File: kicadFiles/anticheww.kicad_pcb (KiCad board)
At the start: 2 copper layers, 303.2 x 94.2 mm, 154 parts, among them J1 TYPE-C-31-M12_13, SW1 ESC, SW10 9, SW11 0, SW12 MINUS, SW13 PLUS, SW14 LBKSP, SW15 RBKSP, SW16 PGUP, SW17 2U_BKSP, SW18 TAB, SW19 Q, SW2 1, SW20 W, SW21 E, SW22 R, SW23 T, SW24 Y, SW25 U, SW26 I, SW27 O, SW28 P, SW29 LBRKT, SW3 2, SW30 RBRKT, SW31 BKSLSH, SW32 PGDN, SW33 CAPS, SW34 A, SW35 S, SW36 D, SW37 F, SW38 G, SW39 H, SW4 3, SW40 J, SW41 K, SW42 L, SW43 COLON, SW44 QUOTE, SW45 ENTER, SW46 HOME, SW47 LSHFT, SW48 STEPPED_CAPS, SW49 Z, SW5 4, SW50 X, SW51 C, SW52 V, SW53 B, SW54 N, SW55 M, SW56 COMMA, SW57 DOT, SW58 175_RSHFT, SW59 UP, SW6 5, SW60 END, SW61 SLSH, SW62 LCTRL, SW63 LGUI, SW64 LALT, SW65 SPC, SW66 RALT, SW67 RGUI, SW68 RCTRL, SW69 LEFT, SW7 6, SW70 DOWN, SW71 RIGHT, SW72 LCTRL, SW73 LGUI, SW74 LALT, SW75 SPC, SW8 7, SW9 8

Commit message: Route USB data lines
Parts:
- added U1: TPD4E05U06DQAR, acheron_Components:USON-10_2.5x1.0mm_P0.5mm, F.Cu at (337.2, 92.4)
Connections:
- J1 pad A6: Net-(J1-PadA6) -> D+
- J1 pad A7: Net-(J1-PadA7) -> D-
- J1 pad B6: Net-(J1-PadB6) -> D+
- J1 pad B7: Net-(J1-PadB7) -> D-
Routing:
- net D-: track 0.00 -> 32.9 mm, vias 0 -> 2
- net D+: track 0.00 -> 30.6 mm, vias 0 -> 2
- net Net-(J1-PadS): track 0.00 -> 17.0 mm
- net GND: track 0.00 -> 5.02 mm, vias 0 -> 3
- added copper zone on B.Cu, net GND
- added copper zone on F.Cu, net GND
- removed copper zone on B.Cu, net (none)
- removed copper zone on F.Cu, net (none)

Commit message: Add RGB
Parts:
- added C1: 100n, Capacitor_SMD:C_0805_2012Metric, F.Cu at (485.9, 334.5)
- added C10: 100n, Capacitor_SMD:C_0805_2012Metric, F.Cu at (287.8, 257.6)
- added C11: 100n, Capacitor_SMD:C_0805_2012Metric, F.Cu at (283.4, 257.6)
- added C12: 100n, Capacitor_SMD:C_0805_2012Metric, F.Cu at (292.2, 257.6)
- added C13: 100n, Capacitor_SMD:C_0805_2012Metric, F.Cu at (283.4, 269.4)
- added C14: 100n, Capacitor_SMD:C_0805_2012Metric, F.Cu at (274.4, 272.3)
- added C2: 100n, Capacitor_SMD:C_0805_2012Metric, F.Cu at (481.5, 340.4)
- added C3: 100n, Capacitor_SMD:C_0805_2012Metric, F.Cu at (477.5, 347.8)
- added C4: 100n, Capacitor_SMD:C_0805_2012Metric, F.Cu at (456.3, 354.4)
- added C5: 100n, Capacitor_SMD:C_0805_2012Metric, F.Cu at (485.9, 340.4)
- added C6: 100n, Capacitor_SMD:C_0805_2012Metric, F.Cu at (485.9, 337.5)
- added C7: 100n, Capacitor_SMD:C_0805_2012Metric, F.Cu at (481.5, 337.5)
- added C8: 100n, Capacitor_SMD:C_0805_2012Metric, F.Cu at (287.8, 260.5)
- added C9: 100n, Capacitor_SMD:C_0805_2012Metric, F.Cu at (283.4, 263.5)
- added D47: 1N4148W, acheron_Components:D_SOD-123, F.Cu at (373.7, 172.5)
- added D71: WS2812C, acheron_Components:LED_WS2812B_5.0x5.0mm_P3.2mm, F.Cu at (317.6, 100.9)
- added D72: WS2812C, acheron_Components:LED_WS2812B_5.0x5.0mm_P3.2mm, F.Cu at (279.5, 100.9)
- added D73: WS2812C, acheron_Components:LED_WS2812B_5.0x5.0mm_P3.2mm, F.Cu at (241.4, 100.9)
- added D74: WS2812C, acheron_Components:LED_WS2812B_5.0x5.0mm_P3.2mm, F.Cu at (203.3, 100.9)
- added D75: WS2812C, acheron_Components:LED_WS2812B_5.0x5.0mm_P3.2mm, F.Cu at (165.2, 100.9)
- added D76: WS2812C, acheron_Components:LED_WS2812B_5.0x5.0mm_P3.2mm, F.Cu at (117.6, 100.9)
- added D77: WS2812C, acheron_Components:LED_WS2812B_5.0x5.0mm_P3.2mm, F.Cu at (86.6, 100.9)
- added D78: WS2812C, acheron_Components:LED_WS2812B_5.0x5.0mm_P3.2mm, F.Cu at (85.4, 158.1)
- added D79: WS2812C, acheron_Components:LED_WS2812B_5.0x5.0mm_P3.2mm, F.Cu at (117.6, 158.1)
- added D80: WS2812C, acheron_Components:LED_WS2812B_5.0x5.0mm_P3.2mm, F.Cu at (165.2, 158.1)
- added D81: WS2812C, acheron_Components:LED_WS2812B_5.0x5.0mm_P3.2mm, F.Cu at (203.3, 158.1)
- added D82: WS2812C, acheron_Components:LED_WS2812B_5.0x5.0mm_P3.2mm, F.Cu at (241.4, 158.1)
- added D83: WS2812C, acheron_Components:LED_WS2812B_5.0x5.0mm_P3.2mm, F.Cu at (281.9, 158.1)
- added D84: WS2812C, acheron_Components:LED_WS2812B_5.0x5.0mm_P3.2mm, F.Cu at (315.2, 158.1)
- added FB1: CBG201209U121T, Inductor_SMD:L_0805_2012Metric, F.Cu at (331.8, 96.2)
- added FB2: CBG201209U121T, Inductor_SMD:L_0805_2012Metric, F.Cu at (341.6, 97.2)
- added GR1: Warning Sign (ISO Enter + LED), acheron_Graphics:warning_sign_3.6x3.2mm, F.Cu at (89.1, 115.0)
- added GR2: Warning Sign (Backspace), acheron_Graphics:warning_sign_3.6x3.2mm, F.Cu at (72.7, 84.5)
- added GR3: Warning Sign (ANSI Enter + ISO Backslash), acheron_Graphics:warning_sign_3.6x3.2mm, F.Cu at (98.7, 120.6)
- added GR4: Warning Sign (7U Space), acheron_Graphics:warning_sign_3.6x3.2mm, F.Cu at (151.4, 173.9)
- added GR5: Warning Sign (Left shift), acheron_Graphics:warning_sign_3.6x3.2mm, F.Cu at (318.0, 139.5)
- added LED1: LED, acheron_Components:LED_THT_2.54mm, F.Cu at (346.2, 96.4)
- added LED10: LED, acheron_Components:LED_THT_2.54mm, F.Cu at (174.7, 96.4)
- added LED11: LED, acheron_Components:LED_THT_2.54mm, F.Cu at (155.7, 96.4)
- added LED12: LED, acheron_Components:LED_THT_2.54mm, F.Cu at (136.6, 96.4)
- added LED13: LED, acheron_Components:LED_THT_2.54mm, F.Cu at (117.6, 96.4)
- added LED14: LED, acheron_Components:LED_THT_2.54mm, F.Cu at (98.5, 96.4)
- added LED15: LED, acheron_Components:LED_THT_2.54mm, F.Cu at (79.5, 96.4)
- added LED16: LED, acheron_Components:LED_THT_2.54mm, F.Cu at (89.0, 96.4)
- added LED17: LED, acheron_Components:LED_THT_2.54mm, F.Cu at (60.4, 96.4)
- added LED18: LED, acheron_Components:LED_THT_2.54mm, F.Cu at (341.4, 115.5)
- added LED19: LED, acheron_Components:LED_THT_2.54mm, F.Cu at (317.6, 115.5)
- added LED2: LED, acheron_Components:LED_THT_2.54mm, F.Cu at (327.1, 96.4)
- added LED20: LED, acheron_Components:LED_THT_2.54mm, F.Cu at (298.6, 115.5)
- added LED21: LED, acheron_Components:LED_THT_2.54mm, F.Cu at (279.5, 115.5)
- added LED22: LED, acheron_Components:LED_THT_2.54mm, F.Cu at (260.5, 115.5)
- added LED23: LED, acheron_Components:LED_THT_2.54mm, F.Cu at (241.4, 115.5)
- added LED24: LED, acheron_Components:LED_THT_2.54mm, F.Cu at (222.4, 115.5)
- added LED25: LED, acheron_Components:LED_THT_2.54mm, F.Cu at (203.3, 115.5)
- added LED26: LED, acheron_Components:LED_THT_2.54mm, F.Cu at (184.3, 115.5)
- added LED27: LED, acheron_Components:LED_THT_2.54mm, F.Cu at (165.2, 115.5)
- added LED28: LED, acheron_Components:LED_THT_2.54mm, F.Cu at (146.2, 115.5)
- added LED29: LED, acheron_Components:LED_THT_2.54mm, F.Cu at (127.1, 115.5)
- added LED3: LED, acheron_Components:LED_THT_2.54mm, F.Cu at (308.1, 96.4)
- added LED30: LED, acheron_Components:LED_THT_2.54mm, F.Cu at (108.1, 115.5)
- added LED31: LED, acheron_Components:LED_THT_2.54mm, F.Cu at (84.2, 115.5)
- added LED32: LED, acheron_Components:LED_THT_2.54mm, F.Cu at (60.4, 115.5)
- added LED33: LED, acheron_Components:LED_THT_2.54mm, F.Cu at (343.8, 134.5)
- added LED34: LED, acheron_Components:LED_THT_2.54mm, F.Cu at (339.0, 134.5)
- added LED35: LED, acheron_Components:LED_THT_2.54mm, F.Cu at (312.8, 134.5)
- added LED36: LED, acheron_Components:LED_THT_2.54mm, F.Cu at (293.8, 134.5)
- added LED37: LED, acheron_Components:LED_THT_2.54mm, F.Cu at (274.7, 134.5)
- added LED38: LED, acheron_Components:LED_THT_2.54mm, F.Cu at (255.7, 134.5)
- added LED39: LED, acheron_Components:LED_THT_2.54mm, F.Cu at (236.6, 134.5)
- added LED4: LED, acheron_Components:LED_THT_2.54mm, F.Cu at (289.0, 96.4)
- added LED40: LED, acheron_Components:LED_THT_2.54mm, F.Cu at (217.6, 134.5)
- added LED41: LED, acheron_Components:LED_THT_2.54mm, F.Cu at (198.5, 134.5)
- added LED42: LED, acheron_Components:LED_THT_2.54mm, F.Cu at (179.5, 134.5)
- added LED43: LED, acheron_Components:LED_THT_2.54mm, F.Cu at (160.4, 134.5)
- added LED44: LED, acheron_Components:LED_THT_2.54mm, F.Cu at (141.4, 134.5)
- added LED45: LED, acheron_Components:LED_THT_2.54mm, F.Cu at (122.3, 134.5)
- added LED46: LED, acheron_Components:LED_THT_2.54mm, F.Cu at (103.3, 134.5)
- added LED47: LED, acheron_Components:LED_THT_2.54mm, F.Cu at (91.4, 134.5)
- added LED48: LED, acheron_Components:LED_THT_2.54mm, F.Cu at (60.4, 134.5)
- added LED49: LED, acheron_Components:LED_THT_2.54mm, F.Cu at (343.8, 153.6)
- added LED5: LED, acheron_Components:LED_THT_2.54mm, F.Cu at (270.0, 96.4)
- added LED50: LED, acheron_Components:LED_THT_2.54mm, F.Cu at (334.3, 153.6)
- added LED51: LED, acheron_Components:LED_THT_2.54mm, F.Cu at (322.4, 153.6)
- added LED52: LED, acheron_Components:LED_THT_2.54mm, F.Cu at (303.3, 153.6)
- added LED53: LED, acheron_Components:LED_THT_2.54mm, F.Cu at (284.3, 153.6)
- added LED54: LED, acheron_Components:LED_THT_2.54mm, F.Cu at (265.2, 153.6)
- added LED55: LED, acheron_Components:LED_THT_2.54mm, F.Cu at (246.2, 153.6)
- added LED56: LED, acheron_Components:LED_THT_2.54mm, F.Cu at (227.1, 153.6)
- added LED57: LED, acheron_Components:LED_THT_2.54mm, F.Cu at (208.1, 153.6)
- added LED58: LED, acheron_Components:LED_THT_2.54mm, F.Cu at (189.0, 153.6)
- added LED59: LED, acheron_Components:LED_THT_2.54mm, F.Cu at (170.0, 153.6)
- added LED6: LED, acheron_Components:LED_THT_2.54mm, F.Cu at (250.9, 96.4)
- added LED60: LED, acheron_Components:LED_THT_2.54mm, F.Cu at (150.9, 153.6)
- added LED61: LED, acheron_Components:LED_THT_2.54mm, F.Cu at (131.9, 153.6)
- added LED62: LED, acheron_Components:LED_THT_2.54mm, F.Cu at (105.7, 153.6)
- added LED63: LED, acheron_Components:LED_THT_2.54mm, F.Cu at (79.5, 153.6)
- added LED64: LED, acheron_Components:LED_THT_2.54mm, F.Cu at (60.4, 153.6)
- added LED65: LED, acheron_Components:LED_THT_2.54mm, F.Cu at (343.8, 172.6)
- added LED66: LED, acheron_Components:LED_THT_2.54mm, F.Cu at (341.4, 172.6)
- added LED67: LED, acheron_Components:LED_THT_2.54mm, F.Cu at (320.0, 172.6)
- added LED68: LED, acheron_Components:LED_THT_2.54mm, F.Cu at (317.6, 172.6)
- added LED69: LED, acheron_Components:LED_THT_2.54mm, F.Cu at (296.2, 172.6)
- added LED7: LED, acheron_Components:LED_THT_2.54mm, F.Cu at (231.9, 96.4)
- added LED70: LED, acheron_Components:LED_THT_2.54mm, F.Cu at (293.8, 172.6)
- added LED71: LED, acheron_Components:LED_THT_2.54mm, F.Cu at (224.7, 172.6)
- added LED72: LED, acheron_Components:LED_THT_2.54mm, F.Cu at (212.8, 172.6)
- added LED73: LED, acheron_Components:LED_THT_2.54mm, F.Cu at (155.7, 172.6)
- added LED74: LED, acheron_Components:LED_THT_2.54mm, F.Cu at (136.6, 172.6)
- added LED75: LED, acheron_Components:LED_THT_2.54mm, F.Cu at (117.6, 172.6)
- added LED76: LED, acheron_Components:LED_THT_2.54mm, F.Cu at (98.5, 172.6)
- added LED77: LED, acheron_Components:LED_THT_2.54mm, F.Cu at (79.5, 172.6)
- added LED78: LED, acheron_Components:LED_THT_2.54mm, F.Cu at (60.4, 172.6)
- added LED79: LED, acheron_Components:LED_THT_2.54mm, F.Cu at (159.8, 226.5)
- added LED8: LED, acheron_Components:LED_THT_2.54mm, F.Cu at (212.8, 96.4)
- added LED80: LED, acheron_Components:LED_THT_2.54mm, F.Cu at (175.9, 220.9)
- added LED9: LED, acheron_Components:LED_THT_2.54mm, F.Cu at (193.8, 96.4)
- added Q1: AO3401A, Package_TO_SOT_SMD:SOT-23, F.Cu at (378.1, 150.2)
- added Q2: DTC123JKAT146, Package_TO_SOT_SMD:SOT-23, F.Cu at (373.6, 150.2)
- added R1: 1k, Resistor_SMD:R_0805_2012Metric, F.Cu at (373.6, 154.0)
- added R10: 420R, Resistor_SMD:R_0805_2012Metric, F.Cu at (365.2, 83.4)
- added R11: 420R, Resistor_SMD:R_0805_2012Metric, F.Cu at (322.4, 97.4)
- added R12: 420R, Resistor_SMD:R_0805_2012Metric, F.Cu at (303.3, 97.4)
- added R13: 420R, Resistor_SMD:R_0805_2012Metric, F.Cu at (384.6, 93.6)
- added R14: 420R, Resistor_SMD:R_0805_2012Metric, F.Cu at (373.9, 102.2)
- added R15: 420R, Resistor_SMD:R_0805_2012Metric, F.Cu at (373.9, 99.2)
- added R16: 420R, Resistor_SMD:R_0805_2012Metric, F.Cu at (382.7, 99.5)
- added R17: 420R, Resistor_SMD:R_0805_2012Metric, F.Cu at (379.2, 96.4)
- added R18: 420R, Resistor_SMD:R_0805_2012Metric, F.Cu at (388.6, 7.95)
- added R19: 420R, Resistor_SMD:R_0805_2012Metric, F.Cu at (387.6, 10.9)
- added R2: 100R, Resistor_SMD:R_0805_2012Metric, F.Cu at (378.0, 154.0)
- added R20: 420R, Resistor_SMD:R_0805_2012Metric, F.Cu at (383.2, 13.7)
- added R21: 420R, Resistor_SMD:R_0805_2012Metric, F.Cu at (392.0, 10.9)
- added R22: 420R, Resistor_SMD:R_0805_2012Metric, F.Cu at (387.6, 13.8)
- added R23: 420R, Resistor_SMD:R_0805_2012Metric, F.Cu at (377.8, 16.4)
- added R24: 420R, Resistor_SMD:R_0805_2012Metric, F.Cu at (382.3, 16.7)
- added R25: 420R, Resistor_SMD:R_0805_2012Metric, F.Cu at (176.0, 64.3)
- added R26: 5R, Resistor_SMD:R_0805_2012Metric, F.Cu at (278.8, 275.2)
- added R27: 5R, Resistor_SMD:R_0805_2012Metric, F.Cu at (287.8, 263.5)
- added R28: 5R, Resistor_SMD:R_0805_2012Metric, F.Cu at (283.4, 266.4)
- added R29: 5R, Resistor_SMD:R_0805_2012Metric, F.Cu at (274.4, 278.2)
- added R3: 5R, Resistor_SMD:R_0805_2012Metric, F.Cu at (473.1, 347.8)
- added R30: 5R, Resistor_SMD:R_0805_2012Metric, F.Cu at (278.8, 272.3)
- added R31: 5R, Resistor_SMD:R_0805_2012Metric, F.Cu at (292.2, 260.5)
- added R32: 5R, Resistor_SMD:R_0805_2012Metric, F.Cu at (283.4, 260.5)
- added R33: 420R, Resistor_SMD:R_0805_2012Metric, F.Cu at (324.2, 42.4)
- added R34: 420R, Resistor_SMD:R_0805_2012Metric, F.Cu at (310.0, 50.8)
- added R35: 420R, Resistor_SMD:R_0805_2012Metric, F.Cu at (319.7, 42.3)
- added R36: 420R, Resistor_SMD:R_0805_2012Metric, F.Cu at (315.3, 42.2)
- added R37: 420R, Resistor_SMD:R_0805_2012Metric, F.Cu at (326.1, 36.5)
- added R38: 420R, Resistor_SMD:R_0805_2012Metric, F.Cu at (320.7, 39.3)
- added R39: 420R, Resistor_SMD:R_0805_2012Metric, F.Cu at (318.8, 45.2)
- added R4: 5R, Resistor_SMD:R_0805_2012Metric, F.Cu at (473.1, 350.7)
- added R40: 420R, Resistor_SMD:R_0805_2012Metric, F.Cu at (314.4, 47.8)
- added R41: 420R, Resistor_SMD:R_0805_2012Metric, F.Cu at (325.1, 39.5)
- added R42: 420R, Resistor_SMD:R_0805_2012Metric, F.Cu at (330.5, 36.5)
- added R43: 420R, Resistor_SMD:R_0805_2012Metric, F.Cu at (310.0, 47.8)
- added R44: 420R, Resistor_SMD:R_0805_2012Metric, F.Cu at (314.4, 50.8)
- added R45: 420R, Resistor_SMD:R_0805_2012Metric, F.Cu at (318.8, 48.2)
- added R46: 420R, Resistor_SMD:R_0805_2012Metric, F.Cu at (360.6, 57.2)
- added R47: 420R, Resistor_SMD:R_0805_2012Metric, F.Cu at (360.6, 60.2)
- added R48: 420R, Resistor_SMD:R_0805_2012Metric, F.Cu at (455.2, 143.5)
- added R49: 420R, Resistor_SMD:R_0805_2012Metric, F.Cu at (449.9, 146.2)
- added R5: 5R, Resistor_SMD:R_0805_2012Metric, F.Cu at (481.5, 334.5)
- added R50: 420R, Resistor_SMD:R_0805_2012Metric, F.Cu at (443.6, 151.8)
- added R51: 420R, Resistor_SMD:R_0805_2012Metric, F.Cu at (459.7, 140.5)
- added R52: 420R, Resistor_SMD:R_0805_2012Metric, F.Cu at (443.6, 154.8)
- added R53: 420R, Resistor_SMD:R_0805_2012Metric, F.Cu at (456.8, 146.4)
- added R54: 420R, Resistor_SMD:R_0805_2012Metric, F.Cu at (459.7, 143.5)
- added R55: 420R, Resistor_SMD:R_0805_2012Metric, F.Cu at (455.2, 140.5)
- added R56: 420R, Resistor_SMD:R_0805_2012Metric, F.Cu at (448.0, 152.1)
- added R57: 420R, Resistor_SMD:R_0805_2012Metric, F.Cu at (452.4, 152.1)
- added R58: 420R, Resistor_SMD:R_0805_2012Metric, F.Cu at (448.0, 149.1)
- added R59: 420R, Resistor_SMD:R_0805_2012Metric, F.Cu at (439.2, 151.8)
- added R6: 5R, Resistor_SMD:R_0805_2012Metric, F.Cu at (465.1, 354.4)
- added R60: 420R, Resistor_SMD:R_0805_2012Metric, F.Cu at (452.4, 149.1)
- added R61: 420R, Resistor_SMD:R_0805_2012Metric, F.Cu at (439.2, 154.8)
- added R62: 420R, Resistor_SMD:R_0805_2012Metric, F.Cu at (328.4, 207.2)
- added R63: 420R, Resistor_SMD:R_0805_2012Metric, F.Cu at (440.4, 39.0)
- added R64: 420R, Resistor_SMD:R_0805_2012Metric, F.Cu at (445.7, 33.4)
- added R65: 420R, Resistor_SMD:R_0805_2012Metric, F.Cu at (450.1, 33.4)
- added R66: 420R, Resistor_SMD:R_0805_2012Metric, F.Cu at (438.5, 47.9)
- added R67: 420R, Resistor_SMD:R_0805_2012Metric, F.Cu at (429.6, 47.5)
- added R68: 420R, Resistor_SMD:R_0805_2012Metric, F.Cu at (450.1, 36.3)
- added R69: 420R, Resistor_SMD:R_0805_2012Metric, F.Cu at (439.4, 44.9)
- added R7: 5R, Resistor_SMD:R_0805_2012Metric, F.Cu at (481.5, 343.4)
- added R70: 420R, Resistor_SMD:R_0805_2012Metric, F.Cu at (443.8, 42.2)
- added R71: 420R, Resistor_SMD:R_0805_2012Metric, F.Cu at (439.4, 42.0)
- added R72: 420R, Resistor_SMD:R_0805_2012Metric, F.Cu at (434.0, 47.8)
- added R73: 420R, Resistor_SMD:R_0805_2012Metric, F.Cu at (443.8, 45.2)
- added R74: 420R, Resistor_SMD:R_0805_2012Metric, F.Cu at (435.0, 44.8)
- added R75: 420R, Resistor_SMD:R_0805_2012Metric, F.Cu at (444.8, 39.3)
- added R76: 420R, Resistor_SMD:R_0805_2012Metric, F.Cu at (445.7, 36.3)
- added R77: 420R, Resistor_SMD:R_0805_2012Metric, F.Cu at (435.0, 41.9)
- added R78: 420R, Resistor_SMD:R_0805_2012Metric, F.Cu at (180.8, 220.9)
- added R79: 420R, Resistor_SMD:R_0805_2012Metric, F.Cu at (180.8, 223.9)
- added R8: 5R, Resistor_SMD:R_0805_2012Metric, F.Cu at (460.7, 354.4)
- added R80: 420R, Resistor_SMD:R_0805_2012Metric, F.Cu at (174.5, 229.5)
- added R81: 420R, Resistor_SMD:R_0805_2012Metric, F.Cu at (185.2, 220.9)
- added R82: 420R, Resistor_SMD:R_0805_2012Metric, F.Cu at (185.2, 223.9)
- added R83: 420R, Resistor_SMD:R_0805_2012Metric, F.Cu at (184.3, 226.8)
- added R84: 420R, Resistor_SMD:R_0805_2012Metric, F.Cu at (175.4, 226.6)
- added R85: 420R, Resistor_SMD:R_0805_2012Metric, F.Cu at (170.1, 232.4)
- added R86: 420R, Resistor_SMD:R_0805_2012Metric, F.Cu at (179.9, 226.8)
- added R87: 420R, Resistor_SMD:R_0805_2012Metric, F.Cu at (178.9, 232.7)
- added R88: 420R, Resistor_SMD:R_0805_2012Metric, F.Cu at (174.5, 232.5)
- added R89: 420R, Resistor_SMD:R_0805_2012Metric, F.Cu at (178.9, 229.8)
- added R9: 5R, Resistor_SMD:R_0805_2012Metric, F.Cu at (490.4, 337.5)
- added R90: 5.1k, Resistor_SMD:R_0805_2012Metric, F.Cu at (340.3, 94.1)
- added R91: 5.1k, Resistor_SMD:R_0805_2012Metric, F.Cu at (334.4, 93.0)
- added SW32: ISO_ENTER, acheron_MX_SolderMask:MX_ISOEnter_Vertical_LED, F.Cu at (81.9, 119.9)
- added SW49: ISO_TILDE, acheron_MX_SolderMask:MX100, F.Cu at (103.3, 129.5)
- added SW51: ISO_BKLSH, acheron_MX_SolderMask:MX100, F.Cu at (322.4, 148.5)
- added SW65: ISO_LSHFT, acheron_MX_SolderMask:MX125, F.Cu at (343.8, 148.5)
- SW45: footprint acheron_MX_SolderMask:MX225R -> acheron_MX_SolderMask:MX225
- moved D4 129.7 mm to (298.6, 91.4), turned to 90 degrees
- moved D3 105.0 mm to (317.6, 91.4), turned to 90 degrees
- renumbered D17 to D16, D18 to D17, D19 to D18, D20 to D19, D21 to D20, D22 to D21, D23 to D22, D24 to D23, D25 to D24, D26 to D25, D27 to D26, D28 to D27, D29 to D28, D30 to D29, D31 to D30, D32 to D31, D33 to D32, D34 to D33, D35 to D34, D36 to D35, D37 to D36, D38 to D37, D39 to D38, D40 to D39, D41 to D40, D42 to D41, D43 to D42, D44 to D43, D45 to D44, D16 to D45, D47 to D48, D48 to D49, D49 to D50, D50 to D51, D51 to D52, D52 to D53, D53 to D54, D54 to D55, D55 to D56, D59 to D57, D56 to D58, D57 to D59, D58 to D60, D60 to D61, D61 to D62, D62 to D63, D63 to D64, D64 to D65, D65 to D66, D66 to D67, D67 to D68, D68 to D69, D69 to D70, H2 to H1, H3 to H2, H4 to H3, H5 to H4, H6 to H5, H7 to H6, H8 to H7, H9 to H8, H10 to H9, SW17 to SW16, SW18 to SW17, SW19 to SW18, SW20 to SW19, SW21 to SW20, SW22 to SW21, SW23 to SW22, SW24 to SW23, SW25 to SW24, SW26 to SW25, SW27 to SW26, SW28 to SW27, SW29 to SW28, SW30 to SW29, SW31 to SW30, SW32 to SW31, SW16 to SW47, SW47 to SW50, SW49 to SW52, SW50 to SW53, SW51 to SW54, SW52 to SW55, SW53 to SW56, SW54 to SW57, SW55 to SW58, SW56 to SW59, SW57 to SW60, SW58 to SW62, SW59 to SW63, SW60 to SW64, SW62 to SW66, SW63 to SW67, SW64 to SW68, SW65 to SW69, SW66 to SW70, SW67 to SW71, SW68 to SW72, SW69 to SW73, SW70 to SW74, SW71 to SW75, SW72 to SW76, SW73 to SW77, SW74 to SW78, SW75 to SW79
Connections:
- D10 pad 1: Net-(D6-Pad1) -> Net-(D1-Pad1)
- D11 pad 1: Net-(D13-Pad1) -> Net-(D1-Pad1)
- D12 pad 1: Net-(D14-Pad1) -> Net-(D1-Pad1)
- D13 pad 1: Net-(D7-Pad1) -> Net-(D1-Pad1)
- D14 pad 1: Net-(D8-Pad1) -> Net-(D1-Pad1)
- D15 pad 1: Net-(D15-Pad1) -> Net-(D1-Pad1)
- D17 pad 1: Net-(D18-Pad1) -> Net-(D17-Pad1)
- D18 pad 1: Net-(D19-Pad1) -> Net-(D17-Pad1)
- D19 pad 1: Net-(D20-Pad1) -> Net-(D17-Pad1)
- D2 pad 1: Net-(D2-Pad1) -> Net-(D1-Pad1)
- D20 pad 1: Net-(D21-Pad1) -> Net-(D17-Pad1)
- D21 pad 1: Net-(D22-Pad1) -> Net-(D17-Pad1)
- D22 pad 1: Net-(D23-Pad1) -> Net-(D17-Pad1)
- D23 pad 1: Net-(D24-Pad1) -> Net-(D17-Pad1)
- D24 pad 1: Net-(D25-Pad1) -> Net-(D17-Pad1)
- D25 pad 1: Net-(D26-Pad1) -> Net-(D17-Pad1)
- D26 pad 1: Net-(D27-Pad1) -> Net-(D17-Pad1)
- D27 pad 1: Net-(D28-Pad1) -> Net-(D17-Pad1)
- D28 pad 1: Net-(D29-Pad1) -> Net-(D17-Pad1)
- D29 pad 1: Net-(D30-Pad1) -> Net-(D17-Pad1)
- D3 pad 1: Net-(D9-Pad1) -> Net-(D1-Pad1)
- D30 pad 1: Net-(D31-Pad1) -> Net-(D17-Pad1)
- D31 pad 1: Net-(D32-Pad1) -> Net-(D16-Pad1)
- D32 pad 1: Net-(D33-Pad1) -> Net-(D16-Pad1)
- D33 pad 1: Net-(D34-Pad1) -> Net-(D16-Pad1)
- D34 pad 1: Net-(D35-Pad1) -> Net-(D16-Pad1)
- D35 pad 1: Net-(D36-Pad1) -> Net-(D16-Pad1)
- D36 pad 1: Net-(D37-Pad1) -> Net-(D16-Pad1)
- D37 pad 1: Net-(D38-Pad1) -> Net-(D16-Pad1)
- D38 pad 1: Net-(D39-Pad1) -> Net-(D16-Pad1)
- D39 pad 1: Net-(D40-Pad1) -> Net-(D16-Pad1)
- D4 pad 1: Net-(D10-Pad1) -> Net-(D1-Pad1)
- D40 pad 1: Net-(D41-Pad1) -> Net-(D16-Pad1)
- D41 pad 1: Net-(D42-Pad1) -> Net-(D16-Pad1)
- D42 pad 1: Net-(D43-Pad1) -> Net-(D16-Pad1)
- D43 pad 1: Net-(D44-Pad1) -> Net-(D16-Pad1)
- D44 pad 1: Net-(D45-Pad1) -> Net-(D16-Pad1)
- D48 pad 1: Net-(D47-Pad1) -> Net-(D46-Pad1)
- D49 pad 1: Net-(D48-Pad1) -> Net-(D46-Pad1)
- D5 pad 1: Net-(D3-Pad1) -> Net-(D1-Pad1)
- D50 pad 1: Net-(D49-Pad1) -> Net-(D46-Pad1)
- D51 pad 1: Net-(D50-Pad1) -> Net-(D46-Pad1)
- D52 pad 1: Net-(D51-Pad1) -> Net-(D46-Pad1)
- D53 pad 1: Net-(D52-Pad1) -> Net-(D46-Pad1)
- D54 pad 1: Net-(D53-Pad1) -> Net-(D46-Pad1)
- D55 pad 1: Net-(D54-Pad1) -> Net-(D46-Pad1)
- D56 pad 1: Net-(D55-Pad1) -> Net-(D46-Pad1)
- D57 pad 1: Net-(D59-Pad1) -> Net-(D46-Pad1)
- D58 pad 1: Net-(D56-Pad1) -> Net-(D46-Pad1)
- D59 pad 1: Net-(D57-Pad1) -> Net-(D46-Pad1)
- D6 pad 1: Net-(D4-Pad1) -> Net-(D1-Pad1)
- D60 pad 1: Net-(D58-Pad1) -> Net-(D46-Pad1)
- D61 pad 2: Net-(D60-Pad2) -> S1
- D62 pad 1: Net-(D61-Pad1) -> Net-(D60-Pad1)
- D62 pad 2: Net-(D61-Pad2) -> S2
- D63 pad 1: Net-(D62-Pad1) -> Net-(D60-Pad1)
- D63 pad 2: Net-(D62-Pad2) -> S3
- D64 pad 1: Net-(D63-Pad1) -> Net-(D60-Pad1)
- D64 pad 2: Net-(D63-Pad2) -> S4
- D65 pad 1: Net-(D64-Pad1) -> Net-(D60-Pad1)
- D66 pad 1: Net-(D65-Pad1) -> Net-(D60-Pad1)
- D67 pad 1: Net-(D66-Pad1) -> Net-(D60-Pad1)
- D68 pad 1: Net-(D67-Pad1) -> Net-(D60-Pad1)
- D69 pad 1: Net-(D68-Pad1) -> Net-(D60-Pad1)
- D7 pad 1: Net-(D11-Pad1) -> Net-(D1-Pad1)
- D70 pad 1: Net-(D69-Pad1) -> Net-(D60-Pad1)
- D8 pad 1: Net-(D12-Pad1) -> Net-(D1-Pad1)
- D9 pad 1: Net-(D5-Pad1) -> Net-(D1-Pad1)
- H1 pad 1: (no net) -> CASE
- H7 pad 1: CASE -> (no net)
- J1 pad A4: Net-(J1-PadA4) -> VBUS
- J1 pad B4: Net-(J1-PadB4) -> VBUS
- SW17 pad 1: Net-(SW18-Pad1) -> Net-(SW1-Pad1)
- SW2 pad 1: Net-(SW2-Pad1) -> Net-(SW19-Pad1)
- SW26 pad 1: Net-(SW27-Pad1) -> Net-(SW10-Pad1)
- SW27 pad 1: Net-(SW28-Pad1) -> Net-(SW11-Pad1)
- SW28 pad 1: Net-(SW29-Pad1) -> Net-(SW12-Pad1)
- SW29 pad 1: Net-(SW30-Pad1) -> Net-(SW13-Pad1)
- SW3 pad 1: Net-(SW3-Pad1) -> Net-(SW20-Pad1)
- SW30 pad 1: Net-(SW31-Pad1) -> Net-(SW14-Pad1)
- SW31 pad 1: Net-(SW32-Pad1) -> Net-(SW15-Pad1)
- SW33 pad 1: Net-(SW33-Pad1) -> Net-(SW1-Pad1)
- SW34 pad 1: Net-(SW34-Pad1) -> Net-(SW19-Pad1)
- SW35 pad 1: Net-(SW35-Pad1) -> Net-(SW20-Pad1)
- SW36 pad 1: Net-(SW36-Pad1) -> Net-(SW21-Pad1)
- SW37 pad 1: Net-(SW37-Pad1) -> Net-(SW22-Pad1)
- SW38 pad 1: Net-(SW38-Pad1) -> Net-(SW23-Pad1)
- SW39 pad 1: Net-(SW39-Pad1) -> Net-(SW24-Pad1)
- SW4 pad 1: Net-(SW4-Pad1) -> Net-(SW21-Pad1)
- SW40 pad 1: Net-(SW40-Pad1) -> Net-(SW25-Pad1)
- SW41 pad 1: Net-(SW41-Pad1) -> Net-(SW26-Pad1)
- SW42 pad 1: Net-(SW42-Pad1) -> Net-(SW10-Pad1)
- SW43 pad 1: Net-(SW43-Pad1) -> Net-(SW11-Pad1)
- SW44 pad 1: Net-(SW44-Pad1) -> Net-(SW12-Pad1)
- SW45 pad 1: Net-(SW45-Pad1) -> Net-(SW13-Pad1)
- SW46 pad 1: Net-(SW46-Pad1) -> Net-(SW14-Pad1)
- SW47 pad 1: Net-(SW17-Pad1) -> Net-(SW15-Pad1)
- SW48 pad 1: Net-(SW33-Pad1) -> Net-(SW1-Pad1)
- SW5 pad 1: Net-(SW5-Pad1) -> Net-(SW22-Pad1)
- SW50 pad 1: Net-(SW47-Pad1) -> Net-(SW1-Pad1)
- SW52 pad 1: Net-(SW49-Pad1) -> Net-(SW20-Pad1)
- SW53 pad 1: Net-(SW50-Pad1) -> Net-(SW21-Pad1)
- SW54 pad 1: Net-(SW51-Pad1) -> Net-(SW22-Pad1)
- SW55 pad 1: Net-(SW52-Pad1) -> Net-(SW23-Pad1)
- SW56 pad 1: Net-(SW53-Pad1) -> Net-(SW24-Pad1)
- SW57 pad 1: Net-(SW54-Pad1) -> Net-(SW25-Pad1)
- SW58 pad 1: Net-(SW55-Pad1) -> Net-(SW26-Pad1)
- SW59 pad 1: Net-(SW56-Pad1) -> Net-(SW10-Pad1)
- SW6 pad 1: Net-(SW6-Pad1) -> Net-(SW23-Pad1)
- SW60 pad 1: Net-(SW57-Pad1) -> Net-(SW11-Pad1)
- SW61 pad 1: Net-(SW61-Pad1) -> Net-(SW12-Pad1)
- SW62 pad 1: Net-(SW58-Pad1) -> Net-(SW13-Pad1)
- SW63 pad 1: Net-(SW59-Pad1) -> Net-(SW14-Pad1)
- SW64 pad 1: Net-(SW60-Pad1) -> Net-(SW15-Pad1)
- SW66 pad 1: Net-(SW62-Pad1) -> Net-(SW1-Pad1)
- SW66 pad 2: Net-(D60-Pad2) -> S1
- SW67 pad 1: Net-(SW63-Pad1) -> Net-(SW19-Pad1)
- SW67 pad 2: Net-(D61-Pad2) -> S2
- SW68 pad 1: Net-(SW64-Pad1) -> Net-(SW20-Pad1)
- SW68 pad 2: Net-(D62-Pad2) -> S3
- SW69 pad 1: Net-(SW65-Pad1) -> Net-(SW23-Pad1)
- SW69 pad 2: Net-(D63-Pad2) -> S4
- SW7 pad 1: Net-(SW7-Pad1) -> Net-(SW24-Pad1)
- SW70 pad 1: Net-(SW66-Pad1) -> Net-(SW10-Pad1)
- SW71 pad 1: Net-(SW67-Pad1) -> Net-(SW11-Pad1)
- SW72 pad 1: Net-(SW68-Pad1) -> Net-(SW12-Pad1)
- SW73 pad 1: Net-(SW69-Pad1) -> Net-(SW13-Pad1)
- SW74 pad 1: Net-(SW70-Pad1) -> Net-(SW14-Pad1)
- SW75 pad 1: Net-(SW71-Pad1) -> Net-(SW15-Pad1)
- SW76 pad 1: Net-(SW72-Pad1) -> Net-(SW1-Pad1)
- SW76 pad 2: Net-(SW72-Pad2) -> S1
- SW77 pad 1: Net-(SW73-Pad1) -> Net-(SW19-Pad1)
- SW77 pad 2: Net-(SW73-Pad2) -> S2
- SW78 pad 1: Net-(SW74-Pad1) -> Net-(SW20-Pad1)
- SW78 pad 2: Net-(SW74-Pad2) -> S3
- SW79 pad 1: Net-(SW75-Pad1) -> Net-(SW23-Pad1)
- SW79 pad 2: Net-(SW75-Pad2) -> S4
- SW8 pad 1: Net-(SW8-Pad1) -> Net-(SW25-Pad1)
- SW9 pad 1: Net-(SW9-Pad1) -> Net-(SW26-Pad1)
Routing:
- net Net-(D1-Pad1): track 0.00 -> 20.2 mm
- net Net-(Q1-Pad3): track 0.00 -> 19.0 mm
- net D+: track 30.6 -> 45.1 mm, vias 2 -> 3
- net CASE: track 0.00 -> 13.8 mm
- net D-: track 32.9 -> 46.0 mm
- net Net-(FB2-Pad2): track 17.0 -> 27.8 mm
- net Net-(D4-Pad2): track 0.00 -> 6.08 mm
- net Net-(D3-Pad2): track 0.00 -> 6.08 mm
- net Net-(J1-PadA5): track 0.00 -> 5.37 mm
- net Net-(J1-PadB5): track 0.00 -> 4.10 mm
- net Net-(LED2-PadA): track 0.00 -> 3.49 mm
- net Net-(LED3-PadA): track 0.00 -> 3.49 mm
- net GND: track 5.02 -> 3.92 mm
- net (no net): vias 0 -> 1
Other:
- net class Default removed
- net class DiffPair removed

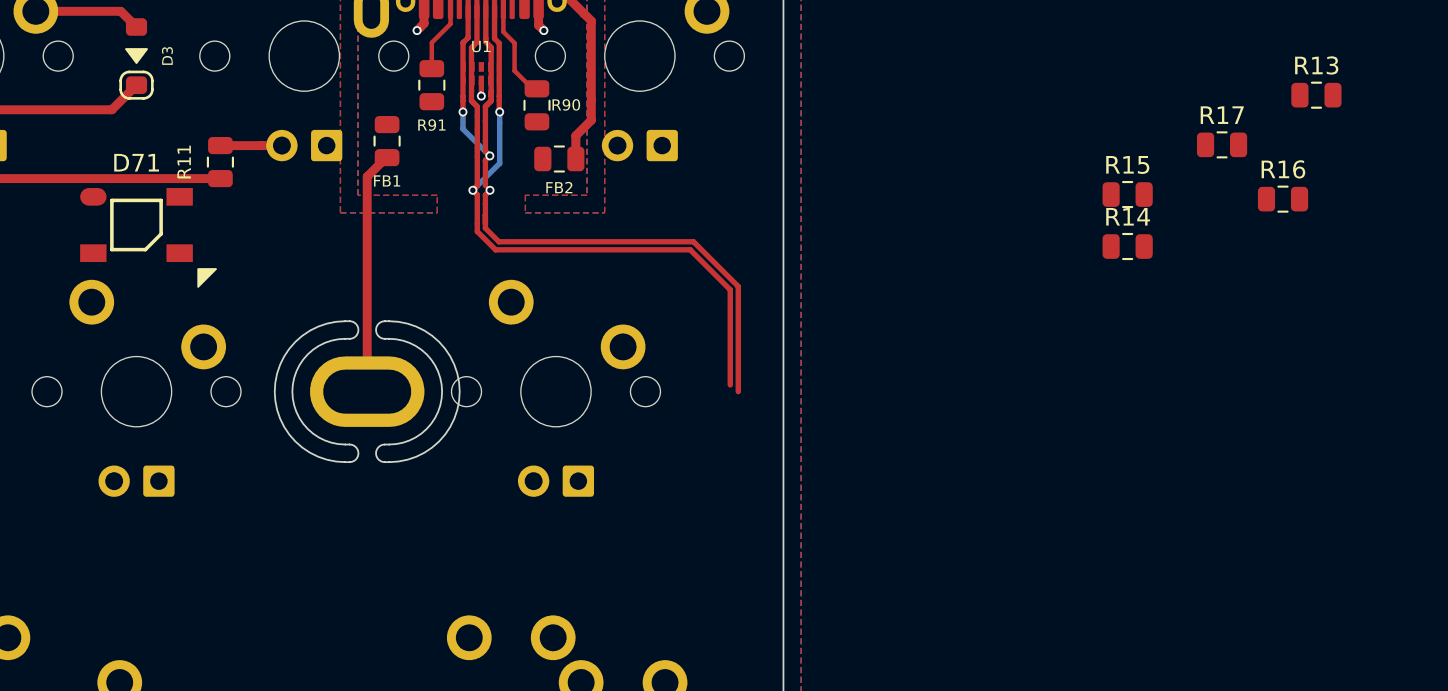
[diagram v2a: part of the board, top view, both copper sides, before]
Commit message: Add level shifter circuit to PCB
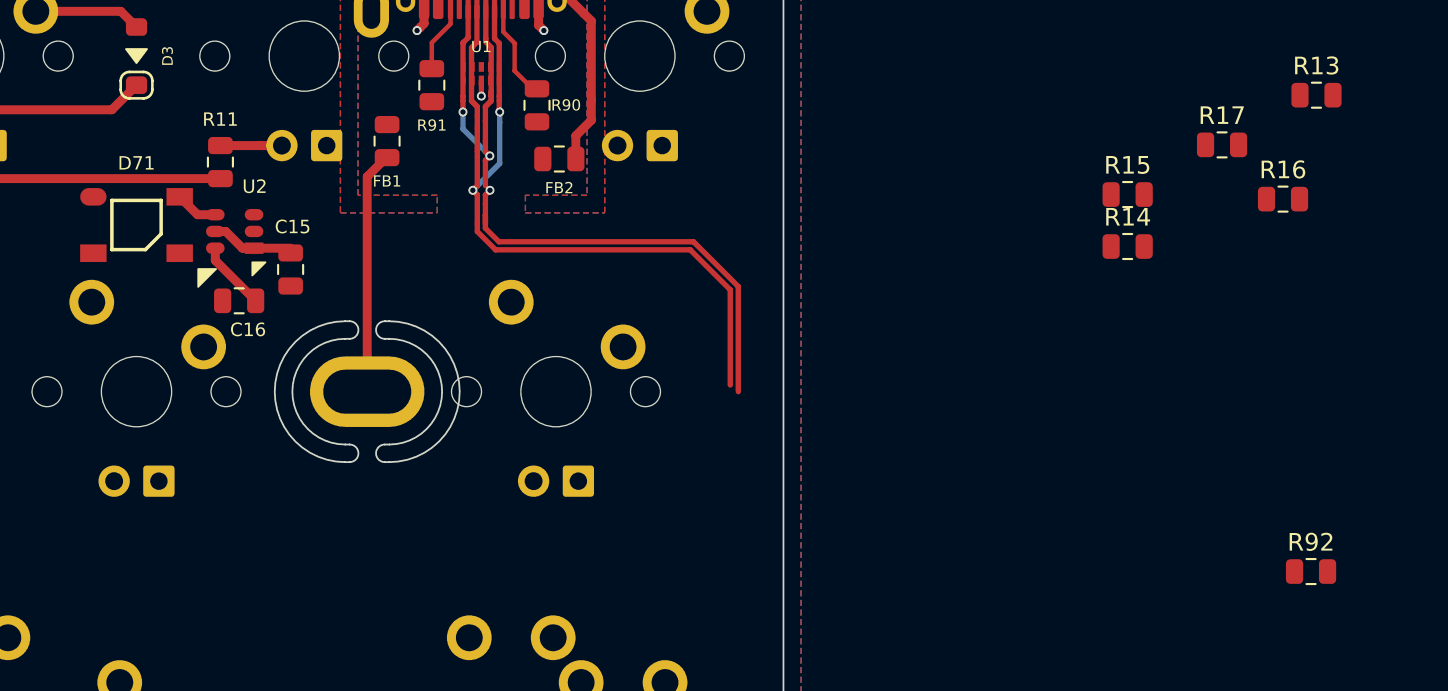
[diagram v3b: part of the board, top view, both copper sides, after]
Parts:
- added C15: 100n, Capacitor_SMD:C_0805_2012Metric, F.Cu at (326.3, 103.5)
- added C16: 100n, Capacitor_SMD:C_0805_2012Metric, F.Cu at (323.4, 105.2)
- added R92: 10k, Resistor_SMD:R_0805_2012Metric, F.Cu at (384.3, 120.6)
- added U2: TXS0101, acheron_Components:SOT-23-6, F.Cu at (323.2, 101.3)
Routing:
- net 3V3: track 0.00 -> 4.67 mm
- net 5V: track 0.00 -> 3.94 mm
- net RGB_5V: track 0.00 -> 2.44 mm

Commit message: Added split space and 2.75 split RShift support
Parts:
- added D85: 1N4148W, acheron_Components:D_SOD-123, F.Cu at (322.4, 248.0)
- added D86: 1N4148W, acheron_Components:D_SOD-123, F.Cu at (335.6, 211.1)
- added LED81: LED, acheron_Components:LED_THT_2.54mm, F.Cu at (96.1, 153.6)
- added LED82: LED, acheron_Components:LED_THT_2.54mm, F.Cu at (220.0, 172.6)
- added LED83: LED, acheron_Components:LED_THT_2.54mm, F.Cu at (229.5, 172.6)
- added LED84: LED, acheron_Components:LED_THT_2.54mm, F.Cu at (262.8, 172.6)
- added LED85: LED, acheron_Components:LED_THT_2.54mm, F.Cu at (258.1, 172.6)
- added LED86: LED, acheron_Components:LED_THT_2.54mm, F.Cu at (191.4, 172.6)
- added LED87: LED, acheron_Components:LED_THT_2.54mm, F.Cu at (186.6, 172.6)
- added R93: 420R, Resistor_SMD:R_0805_2012Metric, F.Cu at (308.4, 264.6)
- added R94: 420R, Resistor_SMD:R_0805_2012Metric, F.Cu at (364.1, 210.9)
- added SW80: 275_RSHFT, acheron_MX_SolderMask:MX275, F.Cu at (96.1, 148.5)
- added SW81: 275_SPC, acheron_MX_SolderMask:MX275R, F.Cu at (258.1, 167.6)
- added SW82: 125_SPC, acheron_MX_SolderMask:MX125, F.Cu at (220.0, 167.6)
- added SW83: 225_SPC, acheron_MX_SolderMask:MX225R, F.Cu at (186.6, 167.6)
- added SW84: 225_SPC, acheron_MX_SolderMask:MX225R, F.Cu at (262.8, 167.6)
- added SW85: SPC, acheron_MX_SolderMask:MX125, F.Cu at (229.5, 167.6)
- added SW86: 275_SPC, acheron_MX_SolderMask:MX275R, F.Cu at (191.4, 167.6)
- added SW87: Rotary_Encoder_Switch_Chassis, acheron_Hardware:ALPS_EC11E, F.Cu at (60.4, 91.4)
- added SW88: Rotary_Encoder_Switch_Chassis, acheron_Hardware:ALPS_EC11E, F.Cu at (60.4, 110.4)
- added SW89: Rotary_Encoder_Switch_Chassis, acheron_Hardware:ALPS_EC11E, F.Cu at (60.4, 129.5)
- added SW90: Rotary_Encoder_Switch_Chassis, acheron_Hardware:ALPS_EC11E, F.Cu at (60.4, 148.5)
- GR3: value Warning Sign (ANSI Enter + ISO Backslash) -> Warning Sign (ANSI Enter + ISO Backslash LED)
- SW45: footprint acheron_MX_SolderMask:MX225 -> acheron_MX_SolderMask:MX225R
- moved D49 373.7 mm to (291.6, 251.4)
- moved D52 367.9 mm to (297.5, 258.1)
- moved D53 356.2 mm to (297.5, 261.4)
- moved D59 356.1 mm to (309.2, 254.7)
- moved D56 350.6 mm to (303.3, 264.8)
- moved D55 350.3 mm to (303.3, 254.7)
- moved D60 349.0 mm to (322.4, 237.9)
- moved D57 348.8 mm to (310.7, 248.0)
- moved D48 344.4 mm to (315.0, 254.7)
- moved D46 343.1 mm to (322.4, 241.3)
- moved D50 326.7 mm to (335.6, 214.4)
- moved D58 320.1 mm to (353.2, 211.1)
- moved D51 314.3 mm to (347.3, 211.1)
- moved D54 314.3 mm to (341.5, 221.1)
- moved D21 251.7 mm to (291.6, 258.1)
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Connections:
- SW79 pad 1: Net-(SW22-Pad1) -> S4
- SW79 pad 2: S4 -> Net-(SW22-Pad1)
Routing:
- net D+: track 45.1 -> 45.2 mm, vias 3 -> 2
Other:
- outline, holes or cut-outs redrawn
- board text added: "(D)"
- board text added: "(S1)"
- board text added: "(S2)"
- board text added: "(T)"
- board text added: "STEPPED"
